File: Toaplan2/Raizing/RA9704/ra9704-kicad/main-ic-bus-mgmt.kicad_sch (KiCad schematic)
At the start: 10 parts, among them U114 E68DEC2 (GAL16V8), U117 PST518A, U118 74AC14, U19 MAIN_IF2 (MACH211), U48 AFBK_CT2 (MACH211), X11 32 MHz

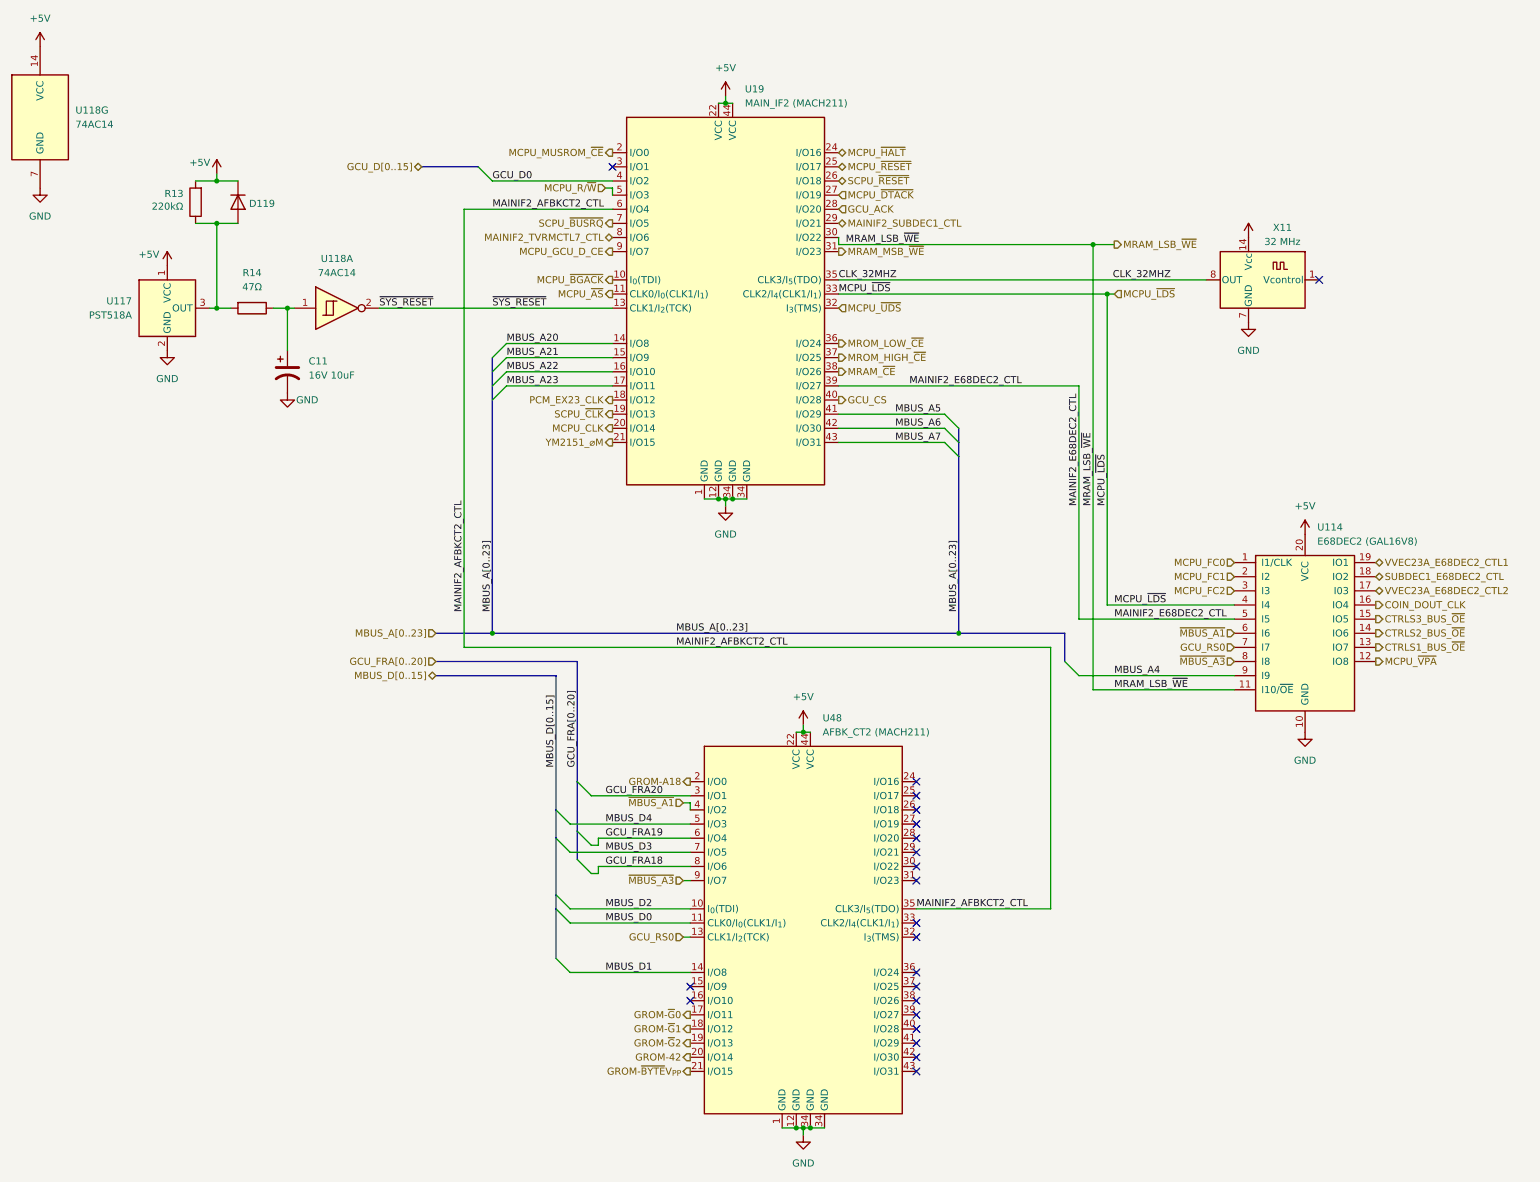
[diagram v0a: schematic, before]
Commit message: fix(ra9704): Add Os as a proxy for 0s in all reference designators
RA9704 has reference designators such that each number has a preceding zero (e.g. RA076, U074, etc.). This causes a bug in KiCAD.

This is 'fixed' by using the 'O' (the letter 'Oh') character instead.

For more info, see the following issue on the KiCAD Gitlab repo

https://gitlab.com/kicad/code/kicad/-/issues/19229
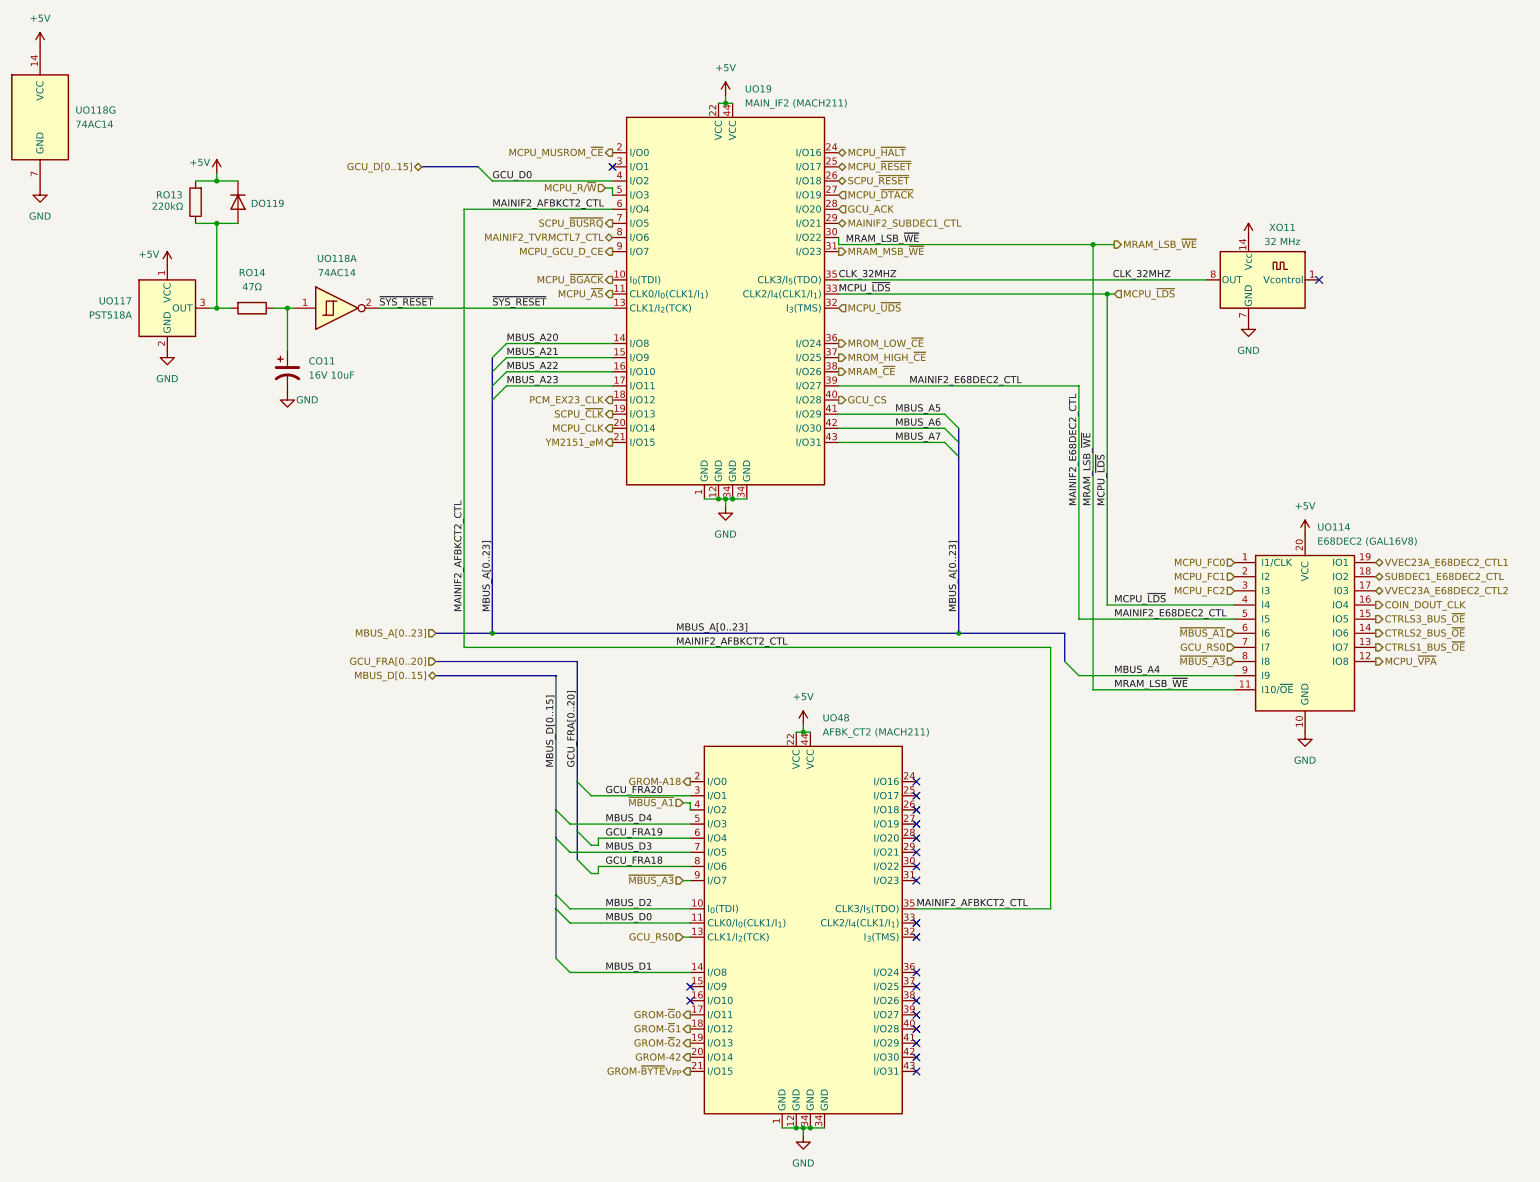
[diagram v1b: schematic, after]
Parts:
- renumbered C11 to CO11, D119 to DO119, R13 to RO13, R14 to RO14, U114 to UO114, U117 to UO117, U118 to UO118, U19 to UO19, U48 to UO48, X11 to XO11
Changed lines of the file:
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@@
 		(dnp no)
 		(fields_autoplaced yes)
-		(property "Reference" "U19"
+		(property "Reference" "UO19"
 			(at 207.9341 49.53 0)
 			(effects
@@
 			(project "ra9704"
 				(path "/24d3b4cf-2360-45fc-8c40-cedc8afdf9e1/f1e08610-acea-4fac-a2bc-d14b9a6056d9"
-					(reference "U19")
+					(reference "UO19")
 					(unit 1)
 				)
@@
 		(on_board yes)
 		(dnp no)
-		(property "Reference" "D119"
-			(at 121.158 70.104 90)
+		(property "Reference" "DO119"
+			(at 122.174 70.104 90)
 			(effects
 				(font
@@
 			(project "ra9704"
 				(path "/24d3b4cf-2360-45fc-8c40-cedc8afdf9e1/f1e08610-acea-4fac-a2bc-d14b9a6056d9"
-					(reference "D119")
+					(reference "DO119")
 					(unit 1)
 				)
@@
 		(dnp no)
 		(fields_autoplaced yes)
-		(property "Reference" "C11"
+		(property "Reference" "CO11"
 			(at 129.54 98.4249 0)
 			(effects
@@
 			(project "ra9704"
 				(path "/24d3b4cf-2360-45fc-8c40-cedc8afdf9e1/f1e08610-acea-4fac-a2bc-d14b9a6056d9"
-					(reference "C11")
+					(reference "CO11")
 					(unit 1)
 				)
@@
 		(on_board yes)
 		(dnp no)
-		(property "Reference" "X11"
+		(property "Reference" "XO11"
 			(at 304.546 74.422 0)
 			(effects
@@
 			(project "ra9704"
 				(path "/24d3b4cf-2360-45fc-8c40-cedc8afdf9e1/f1e08610-acea-4fac-a2bc-d14b9a6056d9"
-					(reference "X11")
+					(reference "XO11")
 					(unit 1)
 				)
@@
 		(dnp no)
 		(fields_autoplaced yes)
-		(property "Reference" "U114"
+		(property "Reference" "UO114"
 			(at 310.8041 128.27 0)
 			(effects
@@
 			(project "ra9704"
 				(path "/24d3b4cf-2360-45fc-8c40-cedc8afdf9e1/f1e08610-acea-4fac-a2bc-d14b9a6056d9"
-					(reference "U114")
+					(reference "UO114")
 					(unit 1)
 				)
@@
 		(dnp no)
 		(fields_autoplaced yes)
-		(property "Reference" "U118"
+		(property "Reference" "UO118"
 			(at 87.63 53.3399 0)
 			(effects
@@
 			(project "ra9704"
 				(path "/24d3b4cf-2360-45fc-8c40-cedc8afdf9e1/f1e08610-acea-4fac-a2bc-d14b9a6056d9"
-					(reference "U118")
+					(reference "UO118")
 					(unit 7)
 				)
@@
 		(on_board yes)
 		(dnp no)
-		(property "Reference" "R13"
-			(at 103.632 68.326 0)
+		(property "Reference" "RO13"
+			(at 102.108 68.58 0)
 			(effects
 				(font
@@
 			(project "ra9704"
 				(path "/24d3b4cf-2360-45fc-8c40-cedc8afdf9e1/f1e08610-acea-4fac-a2bc-d14b9a6056d9"
-					(reference "R13")
+					(reference "RO13")
 					(unit 1)
 				)
@@
 		(dnp no)
 		(fields_autoplaced yes)
-		(property "Reference" "U118"
+		(property "Reference" "UO118"
 			(at 134.62 80.01 0)
 			(effects
@@
 			(project "ra9704"
 				(path "/24d3b4cf-2360-45fc-8c40-cedc8afdf9e1/f1e08610-acea-4fac-a2bc-d14b9a6056d9"
-					(reference "U118")
+					(reference "UO118")
 					(unit 1)
 				)
@@
 		(dnp no)
 		(fields_autoplaced yes)
-		(property "Reference" "R14"
+		(property "Reference" "RO14"
 			(at 119.38 82.55 90)
 			(effects
@@
 			(project "ra9704"
 				(path "/24d3b4cf-2360-45fc-8c40-cedc8afdf9e1/f1e08610-acea-4fac-a2bc-d14b9a6056d9"
-					(reference "R14")
+					(reference "RO14")
 					(unit 1)
 				)
@@
 		(dnp no)
 		(fields_autoplaced yes)
-		(property "Reference" "U48"
+		(property "Reference" "UO48"
 			(at 221.9041 162.56 0)
 			(effects
@@
 			(project "ra9704"
 				(path "/24d3b4cf-2360-45fc-8c40-cedc8afdf9e1/f1e08610-acea-4fac-a2bc-d14b9a6056d9"
-					(reference "U48")
+					(reference "UO48")
 					(unit 1)
 				)
@@
 		(dnp no)
 		(fields_autoplaced yes)
-		(property "Reference" "U117"
+		(property "Reference" "UO117"
 			(at 97.79 87.6299 0)
 			(effects
@@
 			(project "ra9704"
 				(path "/24d3b4cf-2360-45fc-8c40-cedc8afdf9e1/f1e08610-acea-4fac-a2bc-d14b9a6056d9"
-					(reference "U117")
-					(unit 1)
-				)
+					(reference "UO117")
+					(unit 1)
+				)

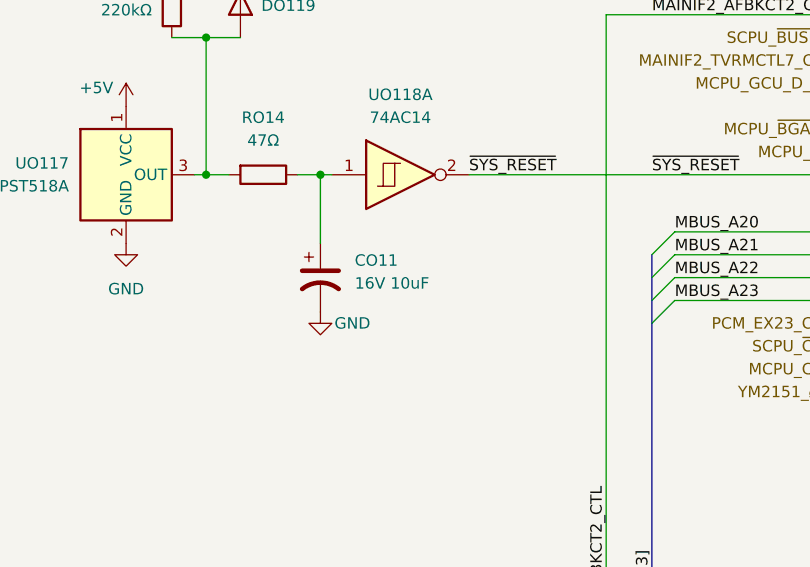
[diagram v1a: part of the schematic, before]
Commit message: doc(ra9704): group 66 ceramic power caps and label on JAMMA page; replace uF with mu symbol
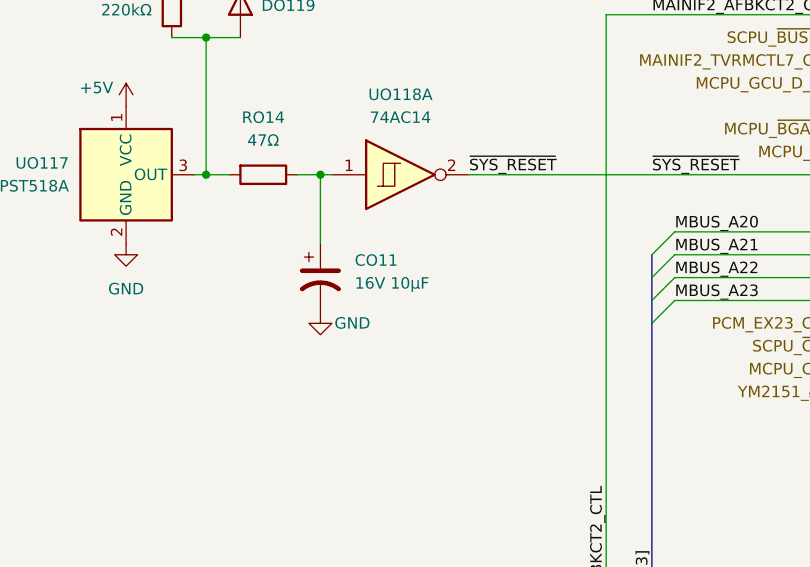
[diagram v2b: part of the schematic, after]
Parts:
- CO11: value 16V 10uF -> 16V 10μF
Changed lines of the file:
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@@
 			)
 		)
-		(property "Value" "16V 10uF"
+		(property "Value" "16V 10μF"
 			(at 129.54 100.9649 0)
 			(effects
